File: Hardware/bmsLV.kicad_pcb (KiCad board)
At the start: 2 copper layers, 121.2 x 60.6 mm, 152 parts, among them J1 Conn_01x06_Male, J10 Conn_01x01_Female, J11 Conn_01x01_Female, J12 Conn_01x01_Female, J13 Conn_01x04_Male, J14 Conn_01x02_Male, J15 Conn_01x02_Male, J16 Conn_01x02_Male, J2 USB_B_Mini, J3 Conn_01x02_Female, J4 Conn_01x02_Male, J5 Conn_01x02_Female, J6 Conn_01x01_Female, J7 Conn_01x01_Female, J8 Conn_01x01_Female, J9 Conn_01x01_Female, K1 RM85V7, Q1 BSS138, Q2 Q_NMOS_GSD, Q3 Q_NMOS_GSD, Q4 Q_NMOS_GSD, Q5 Q_NMOS_GSD, Q6 Q_NMOS_GSD, Q7 Q_NMOS_GSD, Q9 Q_NPN_BCE, SW1 SW_Push, U1 STM32F103C8Tx, U2 LM1117-3.3, U3 LM2596S-5, U4 MCP2562-H-SN, Y1 Crystal

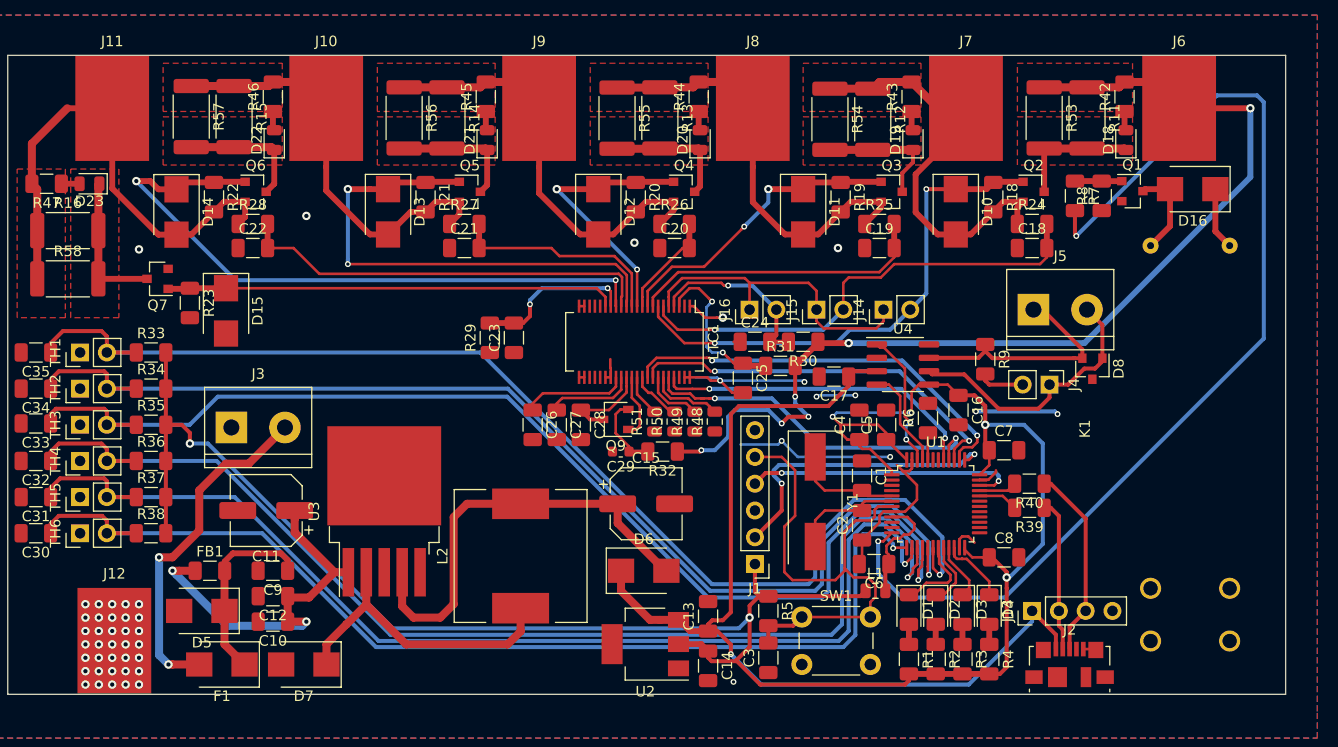
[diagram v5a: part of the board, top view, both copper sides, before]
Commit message: PCB changes + MXCube
-gitignore added to the Hardware and Software sections
-Changed power section wiring on PCB
-MXCube file created as a beginning of Software section
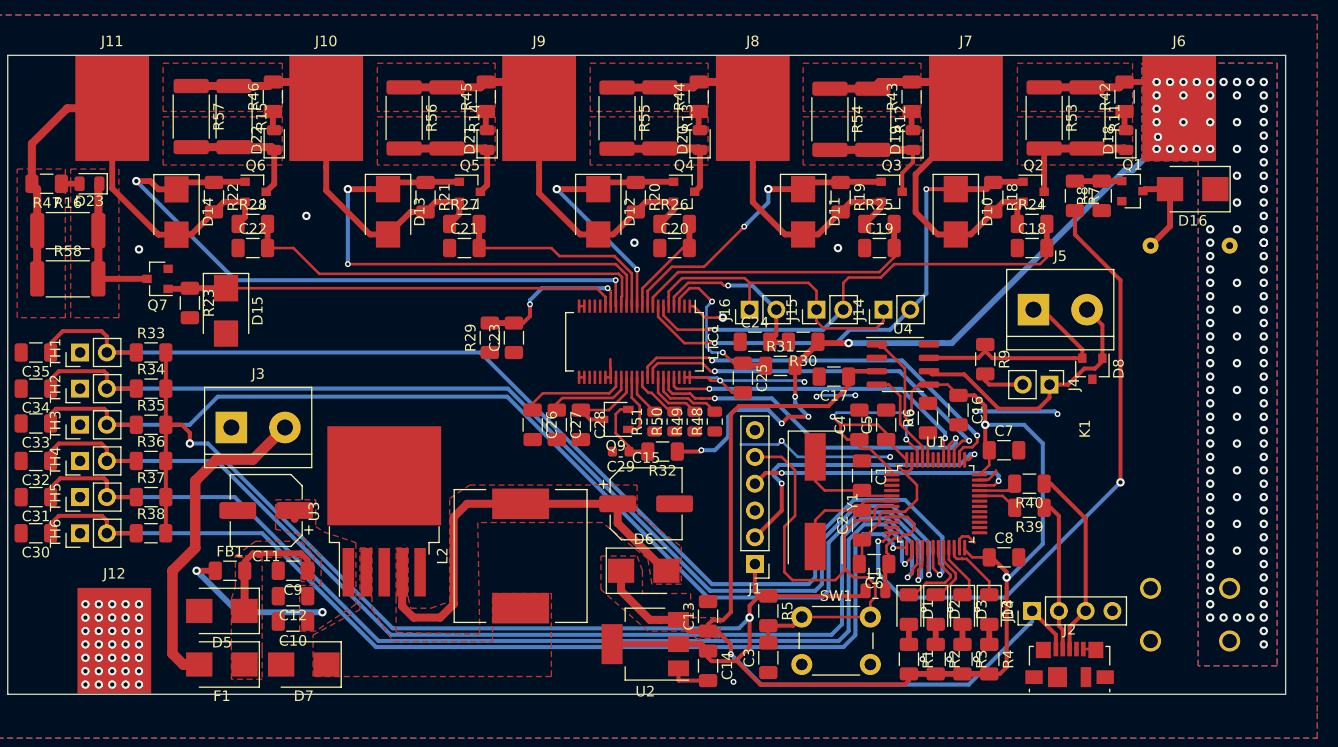
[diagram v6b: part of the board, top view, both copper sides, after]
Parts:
- moved C10 1.91 mm to (45.1, 110.9)
- moved C12 1.91 mm to (45.1, 108.5)
- moved C9 1.91 mm to (45.1, 106.0)
- moved D5 1.91 mm to (38.3, 109.9)
- moved FB1 1.91 mm to (39.1, 106.0)
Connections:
- J6 pad 1: Net-(BT1-Pad1) -> +24V
- R11 pad 1: Net-(BT1-Pad1) -> +24V
- R30 pad 1: Net-(BT1-Pad1) -> +24V
- R31 pad 2: Net-(BT1-Pad1) -> +24V
- R32 pad 1: Net-(BT1-Pad1) -> +24V
- R42 pad 2: Net-(BT1-Pad1) -> +24V
- R53 pad 1: Net-(BT1-Pad1) -> +24V
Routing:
- net Net-(BT1-Pad1): track 99.4 -> 0.00 mm, vias 6 -> 0
- net +24V: track 5.92 -> 78.4 mm, vias 0 -> 120
- net En_Relay: track 100.8 -> 60.7 mm
- net Net-(D7-Pad1): track 29.2 -> 0.00 mm
- net Net-(C10-Pad1): track 35.5 -> 16.1 mm
- net SW_GND: track 71.9 -> 84.5 mm, vias 49 -> 55
- net SW_VDD: track 212.8 -> 219.1 mm
- net Net-(C9-Pad1): track 18.1 -> 12.3 mm
- net VCC: track 32.7 -> 30.9 mm, vias 2 -> 0
- net Net-(D2-Pad1): track 6.21 -> 6.73 mm
- added copper zone on B.Cu, net +24V
- added copper zone on F.Cu, net +24V
- added copper zone on F.Cu, net +5V
- added copper zone on F.Cu, net +5VD
- added copper zone on F.Cu, net Net-(C10-Pad1)
- added copper zone on F.Cu, net Net-(C9-Pad1)
- added copper zone on F.Cu, net Net-(D7-Pad1)
- removed copper zone on F.Cu, net Net-(BT1-Pad1)

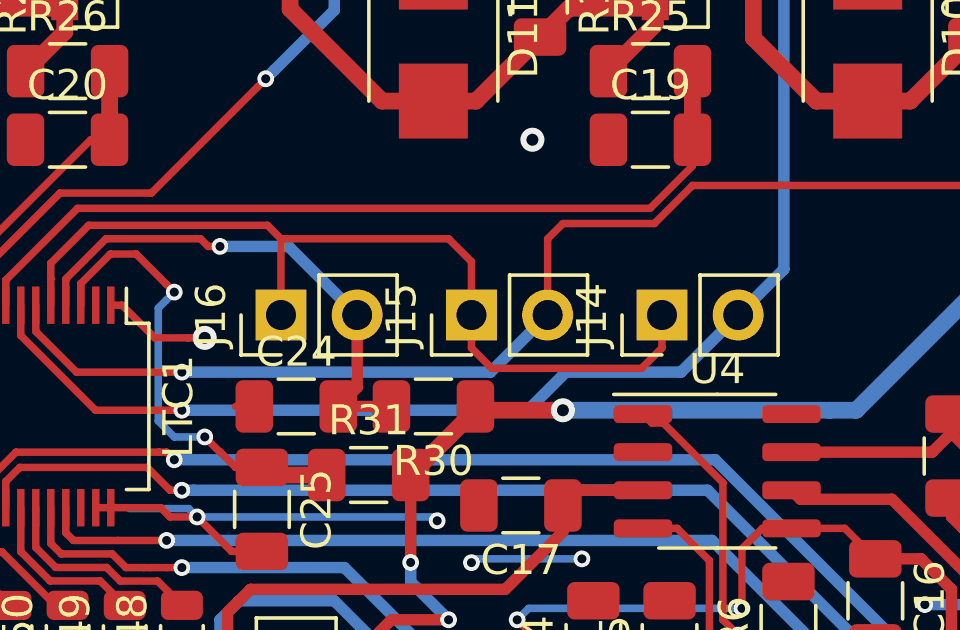
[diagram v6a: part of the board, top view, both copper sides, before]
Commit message: J13, J14, J15 footprint change
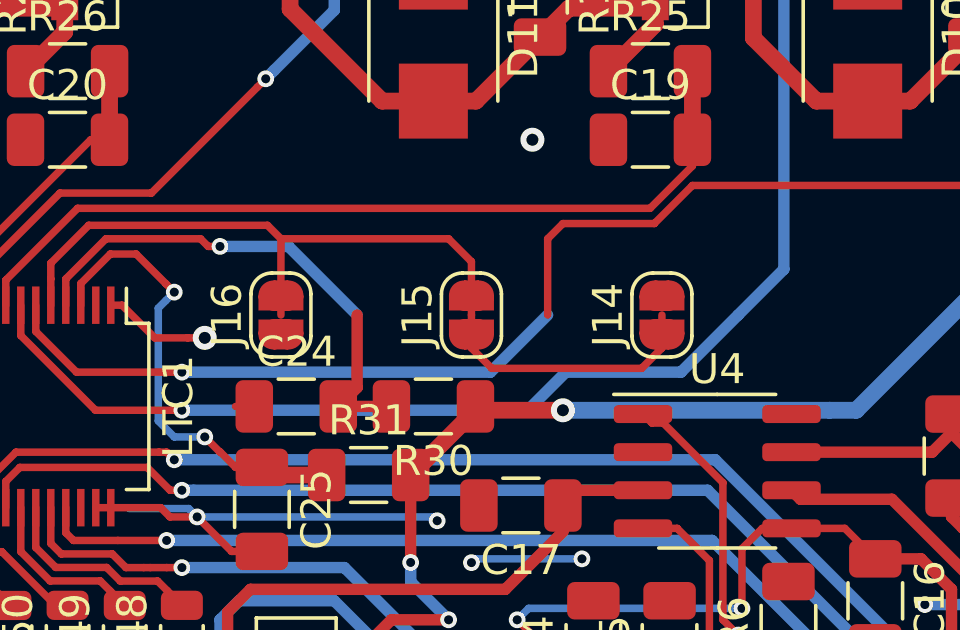
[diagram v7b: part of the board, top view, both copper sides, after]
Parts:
- J14, J15, J16: footprint Connector_PinHeader_2.54mm:PinHeader_1x02_P2.54mm_Vertical -> Jumper:SolderJumper-2_P1.3mm_Open_RoundedPad1.0x1.5mm

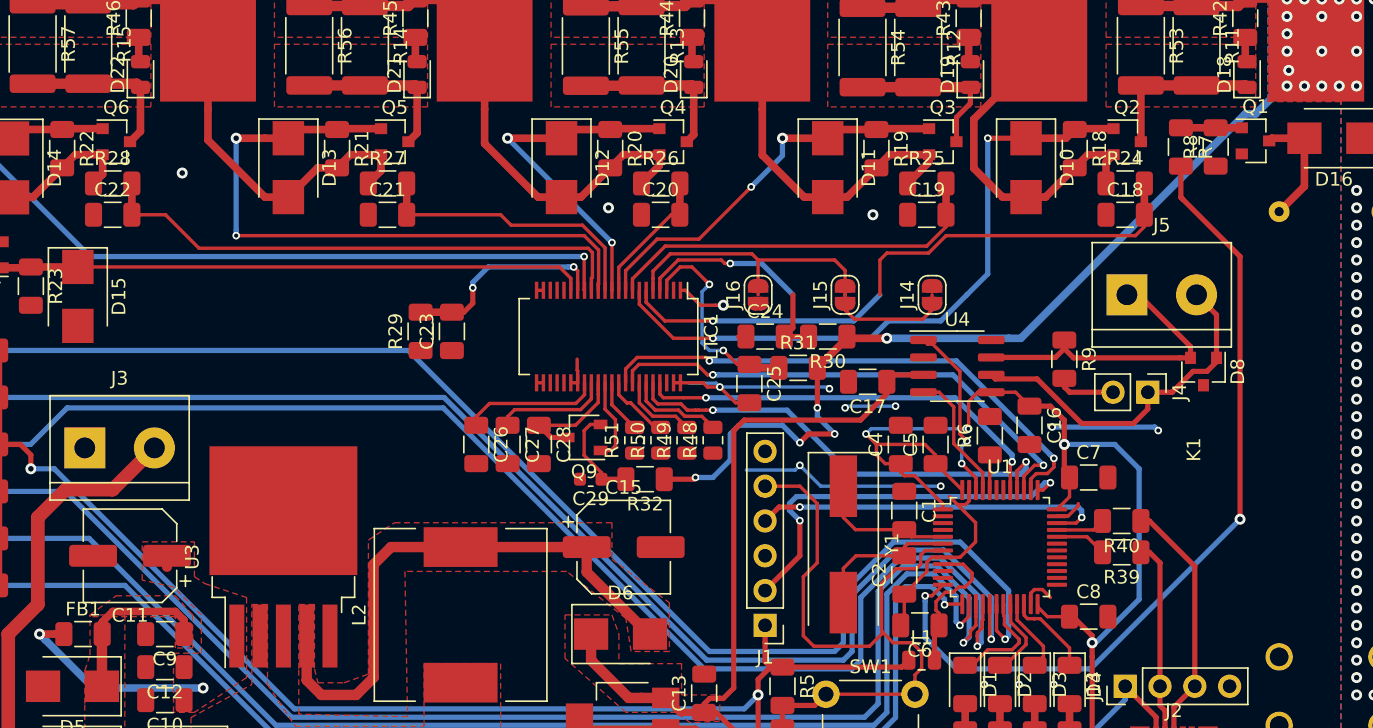
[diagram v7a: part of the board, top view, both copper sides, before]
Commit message: Dash Led and jumpers
-output to Dash Led created
-added another jumper (J17) to ground
-J14, J15, J16 jumper position changed
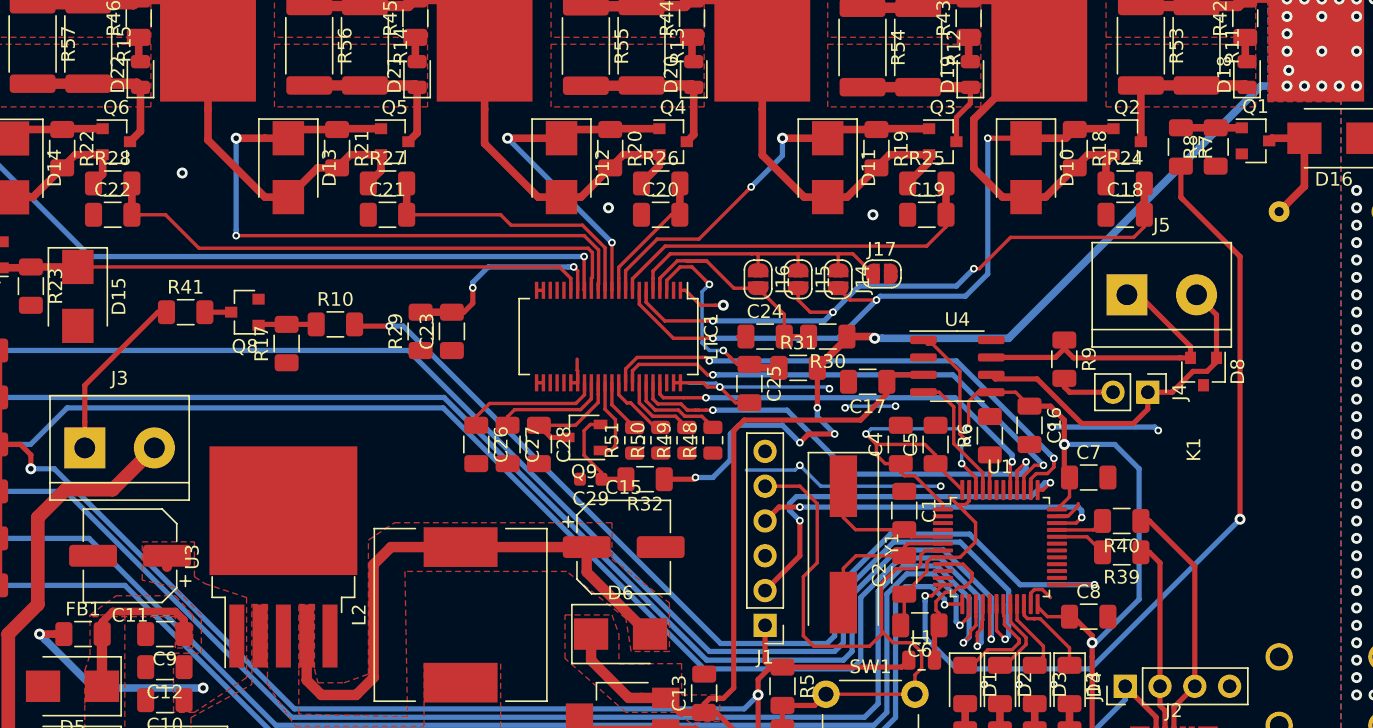
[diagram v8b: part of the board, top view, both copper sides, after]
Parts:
- added J17: Conn_01x02_Male, Jumper:SolderJumper-2_P1.3mm_Open_RoundedPad1.0x1.5mm, F.Cu at (97.4, 79.8)
- added Q8: BSS138, Package_TO_SOT_SMD:SOT-23, F.Cu at (50.9, 82.5)
- added R10: 100, Resistor_SMD:R_1206_3216Metric, F.Cu at (57.5, 83.4)
- added R17: 100K, Resistor_SMD:R_1206_3216Metric, F.Cu at (54.0, 84.8)
- added R41: 30, Resistor_SMD:R_1206_3216Metric, F.Cu at (46.6, 82.5)
- R39, R40: value 27 -> 30
- moved J14 6.95 mm to (94.2, 80.2), turned to 270 degrees
- moved J15 3.61 mm to (91.3, 80.2), turned to 270 degrees
- moved J16 1.13 mm to (88.4, 80.2), turned to 270 degrees
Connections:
- J3 pad 1: SW_GND -> LED_D_OUT
- U1 pad 25: Net-(U1-Pad25) -> LED_D
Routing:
- net LED_D: track 0.00 -> 73.2 mm, vias 0 -> 2
- net LED_D_OUT: track 0.00 -> 12.7 mm
- net Net-(J14-Pad1): track 29.9 -> 22.3 mm
- net Net-(Q8-Pad1): track 0.00 -> 4.23 mm
- net Net-(D10-Pad1): track 48.8 -> 51.9 mm, vias 2 -> 3
- net Net-(C18-Pad2): track 45.3 -> 47.6 mm, vias 1 -> 3
- net Net-(Q8-Pad3): track 0.00 -> 1.92 mm
- net Net-(C24-Pad2): track 17.3 -> 17.0 mm, vias 1 -> 0
